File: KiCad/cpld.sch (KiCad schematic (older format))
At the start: 1 part, among them U8 XC9572XL-VQFP44

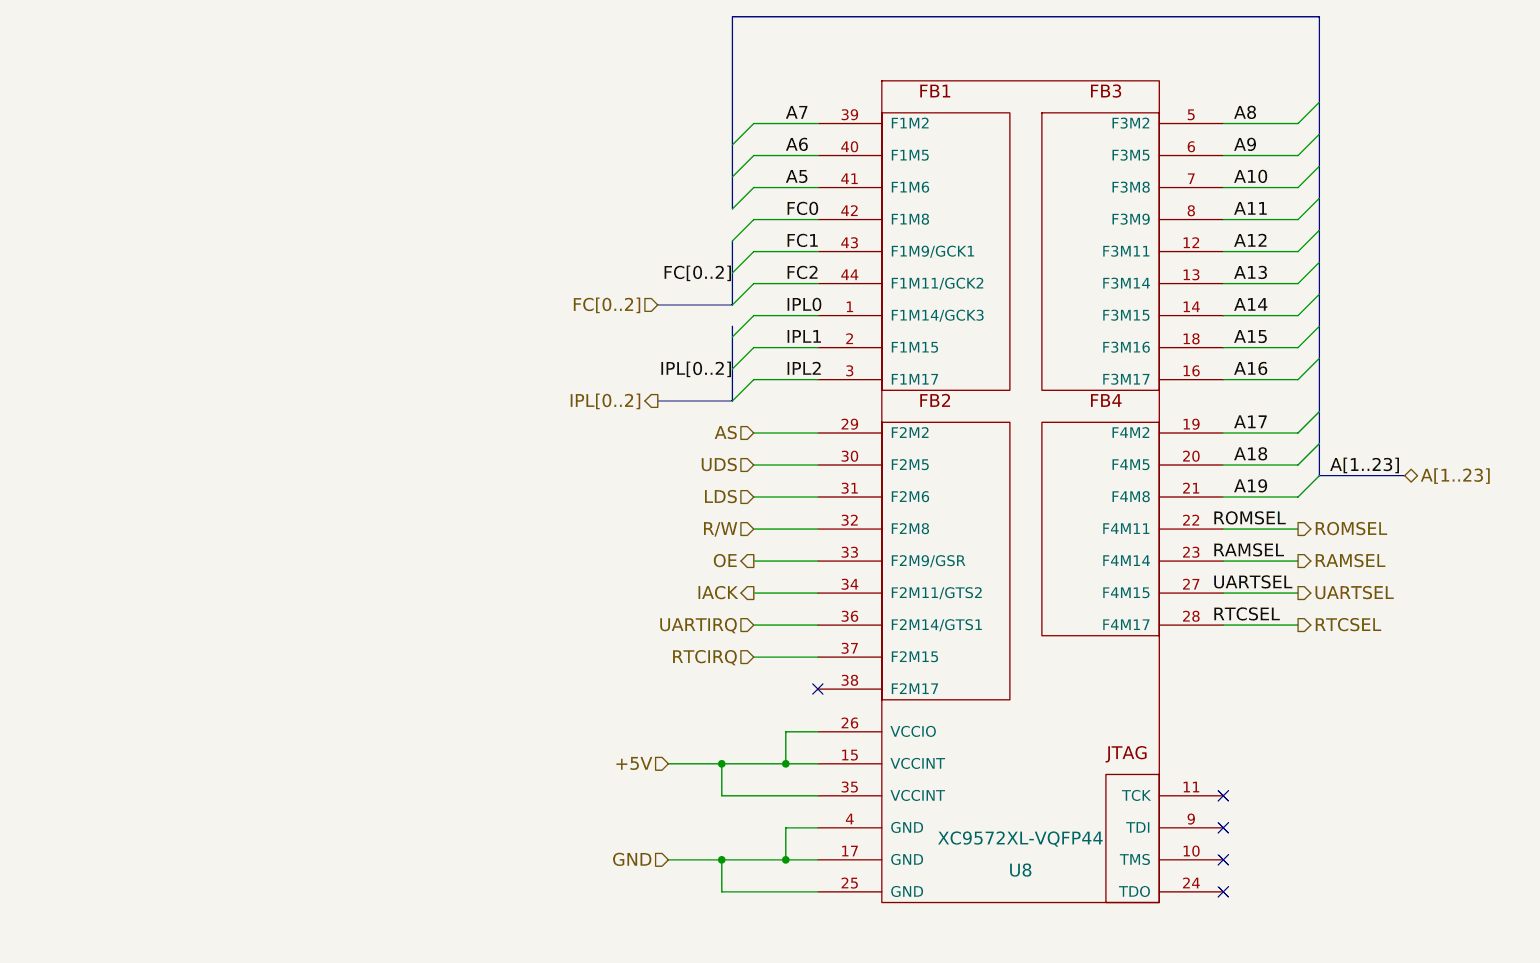
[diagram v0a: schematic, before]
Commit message: begin update for schematic
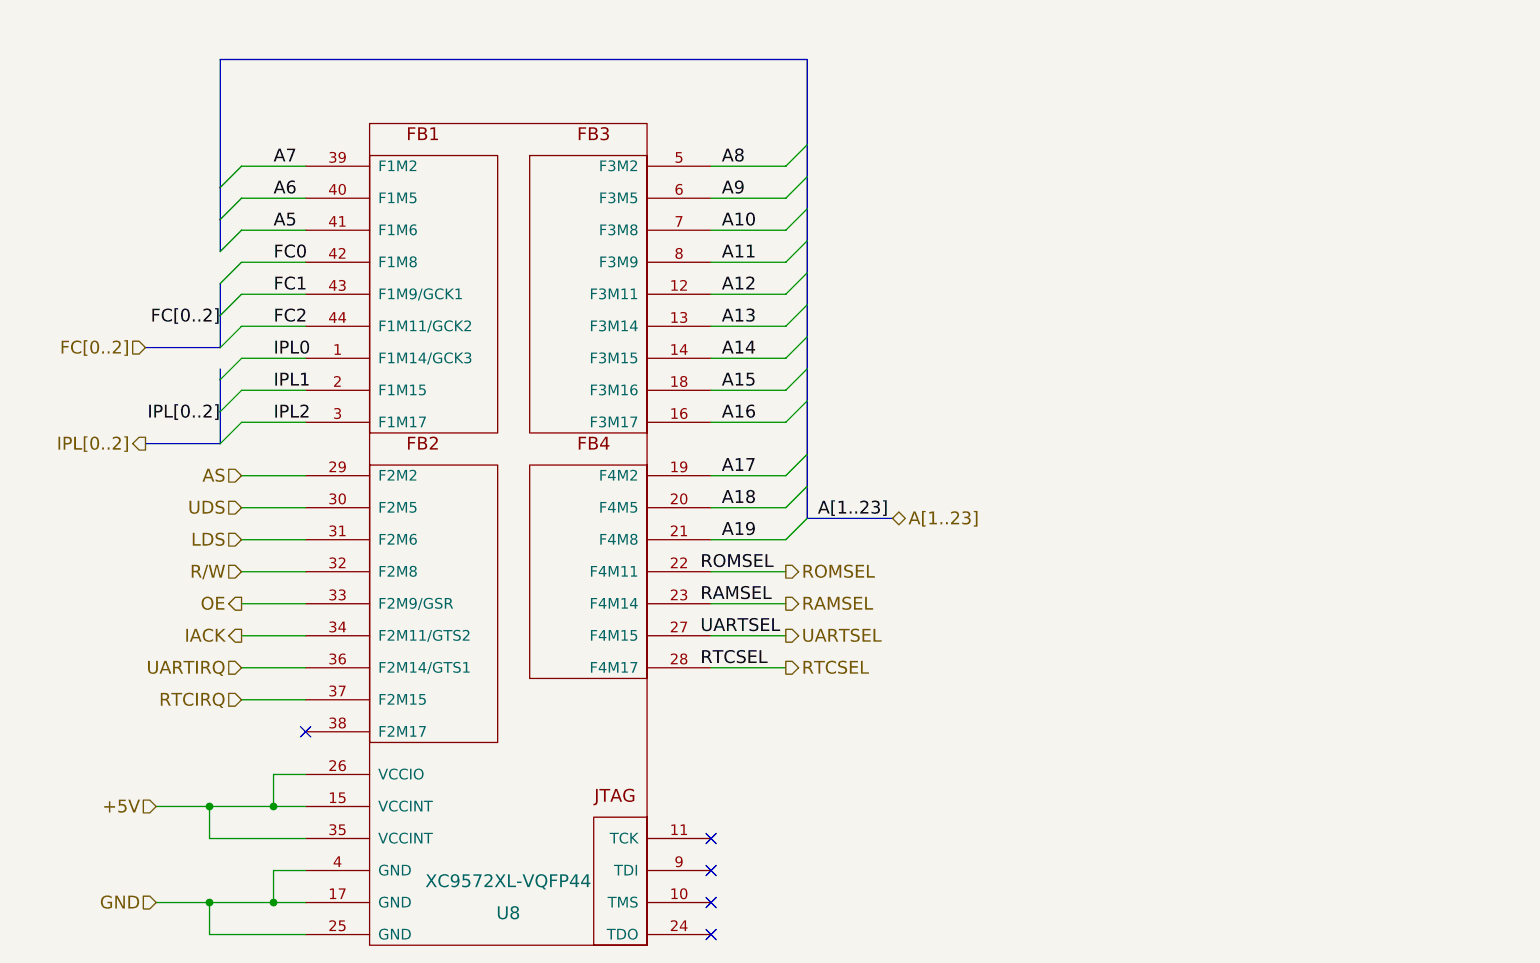
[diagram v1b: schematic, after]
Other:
- moved on the sheet: U8
